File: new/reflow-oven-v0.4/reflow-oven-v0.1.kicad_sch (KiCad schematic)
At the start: 15 parts, among them IC1 MBED-LPC1768, J1 Pot, J2 Conn_01x08_Female, J3 Conn_01x01_Female, J4 Conn_01x01_Female, J5 Conn_01x05_Female, SW1 SW_Push, U1 MOC3041M

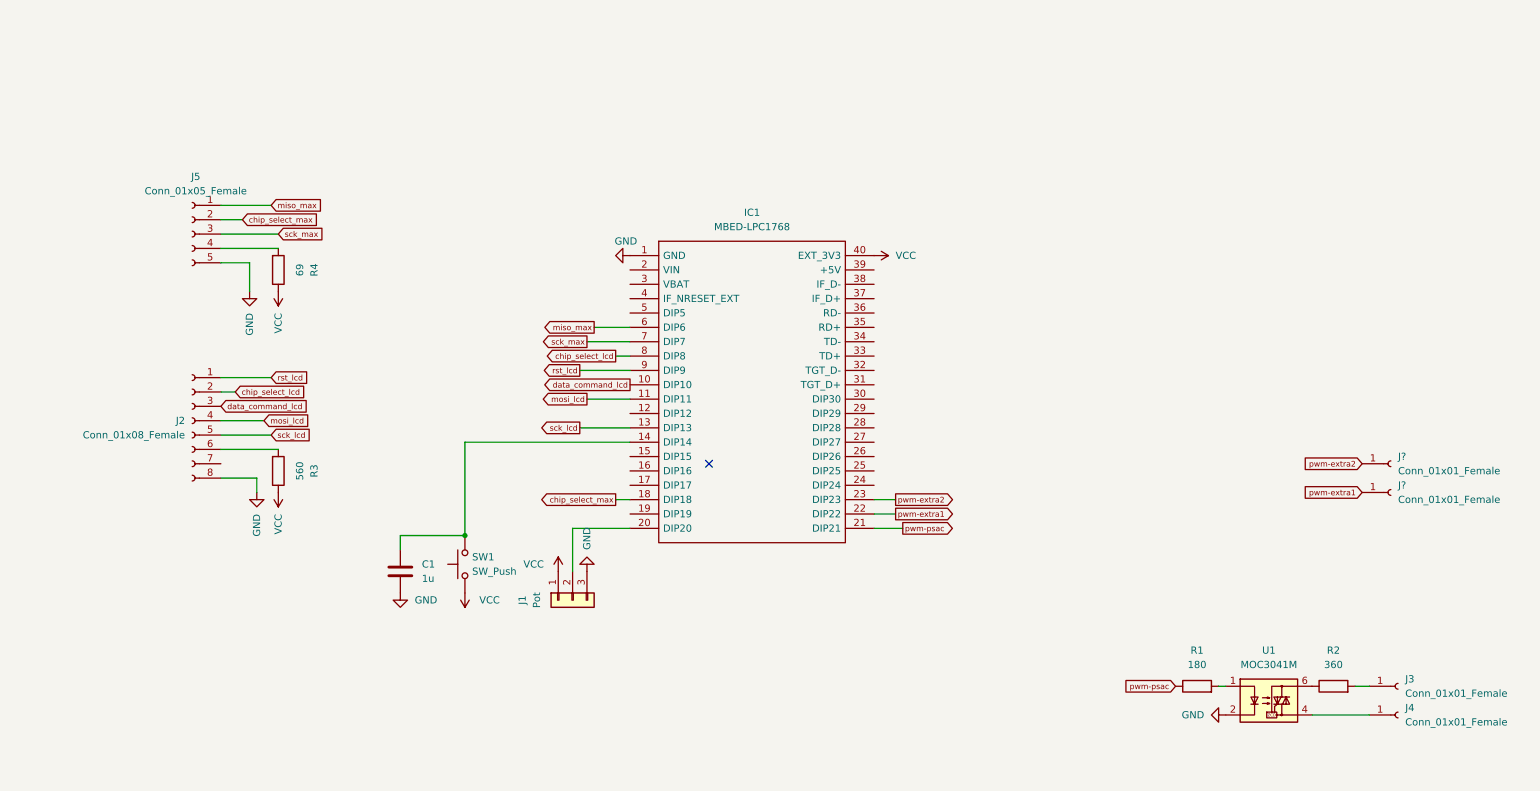
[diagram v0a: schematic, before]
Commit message: Adjusted postion of eletronic components and added push buttons into cad schematic file
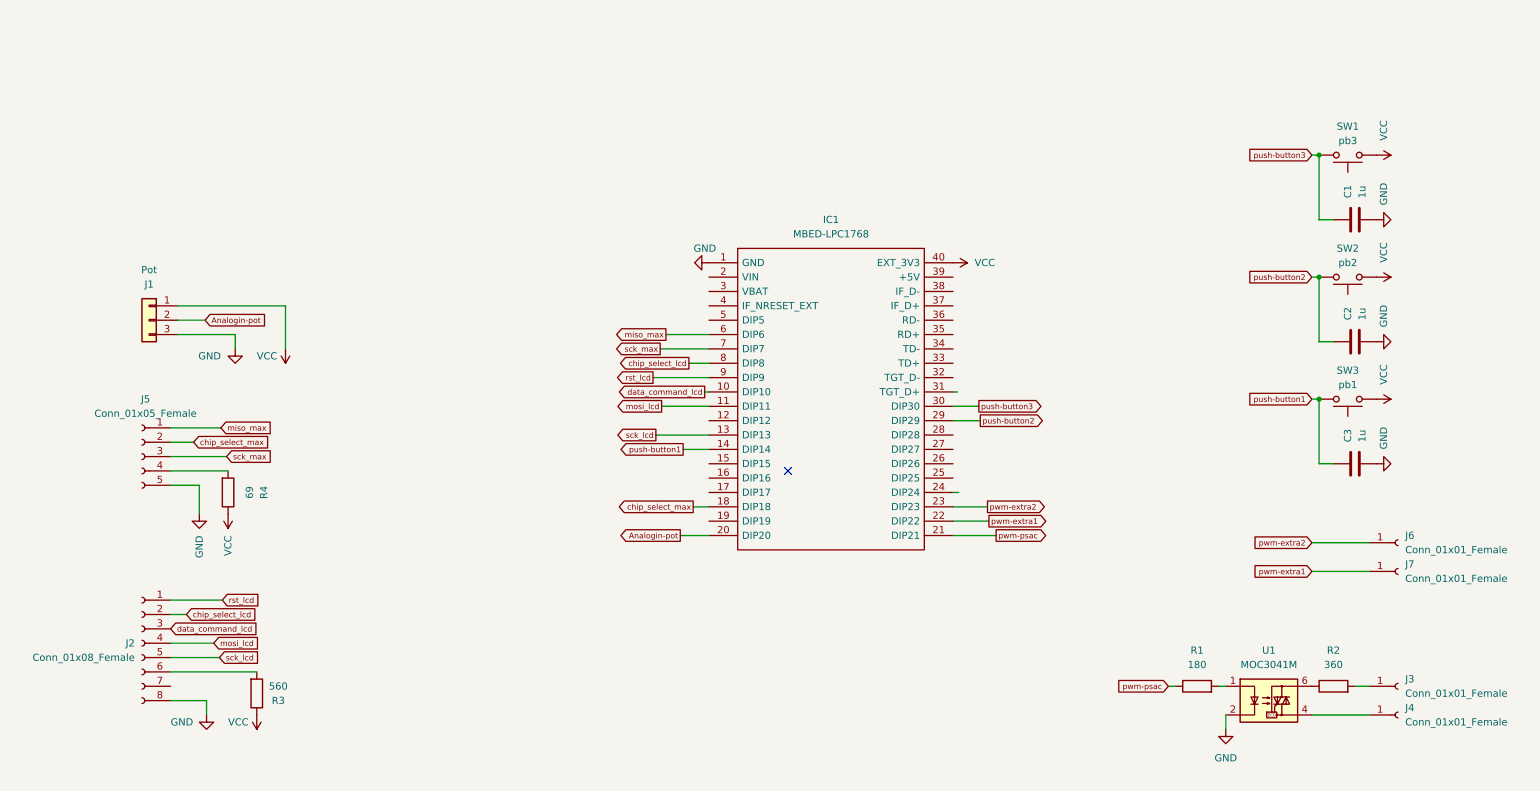
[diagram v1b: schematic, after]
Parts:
- added C2, C3: 1u, symbol Device:C
- added SW2: pb2, symbol Switch:SW_Push
- added SW3: pb1, symbol Switch:SW_Push
- SW1: value SW_Push -> pb3
- gave numbers to parts that had none: 2
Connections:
- net GND: now also C2.2, C3.2
- net VCC: now also SW2.1, SW3.1
- net push-button3: now reaches C1.1, SW1.2
- net push-button3: now also IC1.30 (DIP30); no longer IC1.14 (DIP14)
- net Analogin-pot: now reaches IC1.20 (DIP20), J1.2 (Pin_2)
- net push-button2: now reaches IC1.29 (DIP29)
- net push-button2: now also C2.1, SW2.2
- new net push-button1: C3.1, IC1.14 (DIP14), SW3.2
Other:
- moved on the sheet: IC1, J1, J2, J5, J6, J7, R3, R4

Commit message: Added PCB schematic for prototyping
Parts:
- C1, C2, C3: footprint (none) -> Capacitor_SMD:C_0805_2012Metric_Pad1.18x1.45mm_HandSolder
- J2: footprint (none) -> Connector_PinHeader_2.54mm:PinHeader_1x08_P2.54mm_Vertical
- J5: footprint (none) -> Connector_PinHeader_2.54mm:PinHeader_1x05_P2.54mm_Vertical
- SW1: value pb3 -> pb1; footprint (none) -> Button_Switch_THT:SW_TH_Tactile_Omron_B3F-10xx
- SW2: footprint (none) -> Button_Switch_THT:SW_TH_Tactile_Omron_B3F-10xx
- SW3: value pb1 -> pb3; footprint (none) -> Button_Switch_THT:SW_TH_Tactile_Omron_B3F-10xx
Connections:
- net GND: no longer C1.2, C2.2, C3.2
- net push-button1: now also C1.1, IC1.26 (DIP26); no longer C3.1, IC1.14 (DIP14), SW3.2
- net push-button2: no longer SW2.2
- net push-button3: now also C3.1; no longer C1.1, SW1.2
- new net: C1.2, SW1.2
- new net: C2.2, SW2.2
- new net: C3.2, SW3.2
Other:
- moved on the sheet: C3, SW3

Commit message: Update schematic
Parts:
- SW1, SW2, SW3: footprint Button_Switch_THT:SW_TH_Tactile_Omron_B3F-10xx -> Button_Switch_THT:SW_Tactile_SKHH_Angled
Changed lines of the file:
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@@
     (property "Reference" "SW1" (id 0) (at 260.35 78.74 0))
     (property "Value" "pb1" (id 1) (at 260.35 81.28 0))
-    (property "Footprint" "Button_Switch_THT:SW_TH_Tactile_Omron_B3F-10xx" (id 2) (at 260.35 88.9 0)
+    (property "Footprint" "Button_Switch_THT:SW_Tactile_SKHH_Angled" (id 2) (at 260.35 88.9 0)
       (effects (font (size 1.27 1.27)) hide)
     )
@@
     (property "Reference" "SW2" (id 0) (at 260.35 88.9 0))
     (property "Value" "pb2" (id 1) (at 260.35 91.44 0))
-    (property "Footprint" "Button_Switch_THT:SW_TH_Tactile_Omron_B3F-10xx" (id 2) (at 260.35 99.06 0)
+    (property "Footprint" "Button_Switch_THT:SW_Tactile_SKHH_Angled" (id 2) (at 260.35 99.06 0)
       (effects (font (size 1.27 1.27)) hide)
     )
@@
     (property "Reference" "SW3" (id 0) (at 260.35 100.33 0))
     (property "Value" "pb3" (id 1) (at 260.35 102.87 0))
-    (property "Footprint" "Button_Switch_THT:SW_TH_Tactile_Omron_B3F-10xx" (id 2) (at 260.35 110.49 0)
+    (property "Footprint" "Button_Switch_THT:SW_Tactile_SKHH_Angled" (id 2) (at 260.35 110.49 0)
       (effects (font (size 1.27 1.27)) hide)
     )
@@
     )
     (path "/10e528d8-0539-4f56-b179-694047fd1203"
-      (reference "SW1") (unit 1) (value "pb1") (footprint "Button_Switch_THT:SW_TH_Tactile_Omron_B3F-10xx")
+      (reference "SW1") (unit 1) (value "pb1") (footprint "Button_Switch_THT:SW_Tactile_SKHH_Angled")
     )
     (path "/3e4dfc20-dde8-4357-85d4-9f16e3a1152a"
-      (reference "SW2") (unit 1) (value "pb2") (footprint "Button_Switch_THT:SW_TH_Tactile_Omron_B3F-10xx")
+      (reference "SW2") (unit 1) (value "pb2") (footprint "Button_Switch_THT:SW_Tactile_SKHH_Angled")
     )
     (path "/e7065683-54d8-46fa-9cad-dbded39d791a"
-      (reference "SW3") (unit 1) (value "pb3") (footprint "Button_Switch_THT:SW_TH_Tactile_Omron_B3F-10xx")
+      (reference "SW3") (unit 1) (value "pb3") (footprint "Button_Switch_THT:SW_Tactile_SKHH_Angled")
     )
     (path "/084b209c-133e-4f7d-8446-c65e971f927c"

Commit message: Update schematic
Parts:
- added D?: BTA40-600B, symbol Device:Q_TRIAC_A1A2G
- added F?: Fuse, symbol Device:Fuse
- added R5, R6, R7: 2k, Resistor_SMD:R_0805_2012Metric_Pad1.20x1.40mm_HandSolder, symbol Device:R
- added SW?: SW_MEC_5G, symbol Switch:SW_MEC_5G
- J3: value Conn_01x01_Female -> In-220VAC
- J4: value Conn_01x01_Female -> Out-220VAC
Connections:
- net GND: now also C1.1, C2.1, C3.1
- net push-button1: now also R5.2; no longer C1.1
- net push-button2: now also R6.2; no longer C2.1
- net push-button3: now also R7.2; no longer C3.1
- net at C1.2, SW1.2: now also R5.1
- net at C2.2, SW2.2: now also R6.1
- net at C3.2, SW3.2: now also R7.1
- new net: SW?.1 (A), SW?.2 (A)
- new net: SW?.3 (B), SW?.4 (B)
- new net: D?.2 (A2), F?.2
- new net AC: F?.1
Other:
- note added: "Part-AC"
- note added: "Vin-oven"
- moved on the sheet: C1, J3, J4, R1, R2, R3, SW1, U1
